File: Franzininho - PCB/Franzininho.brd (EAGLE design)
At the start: 51.6 x 24.1 mm, 16 parts, among them IC1 TINY45-20-DIP, X1 USBPCB

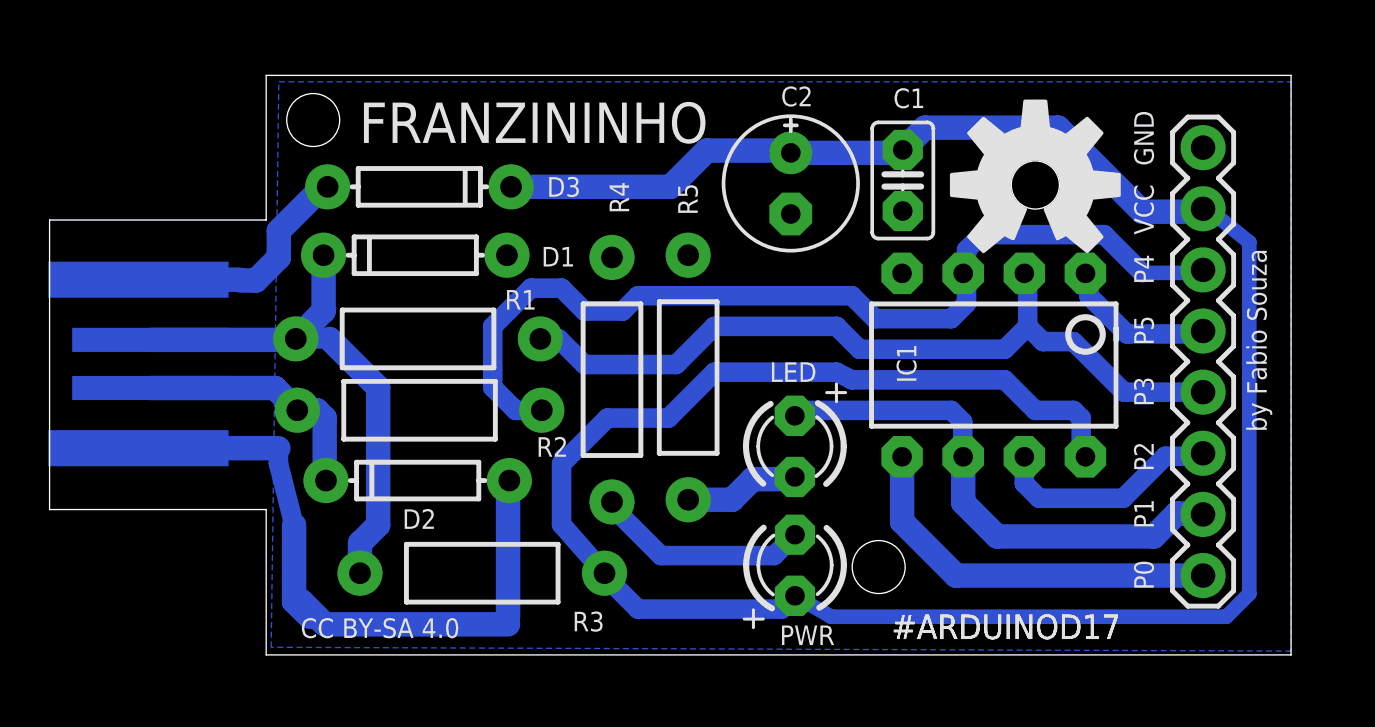
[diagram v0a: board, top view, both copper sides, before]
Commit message: update
aumentado um pouco o tamanho da placa
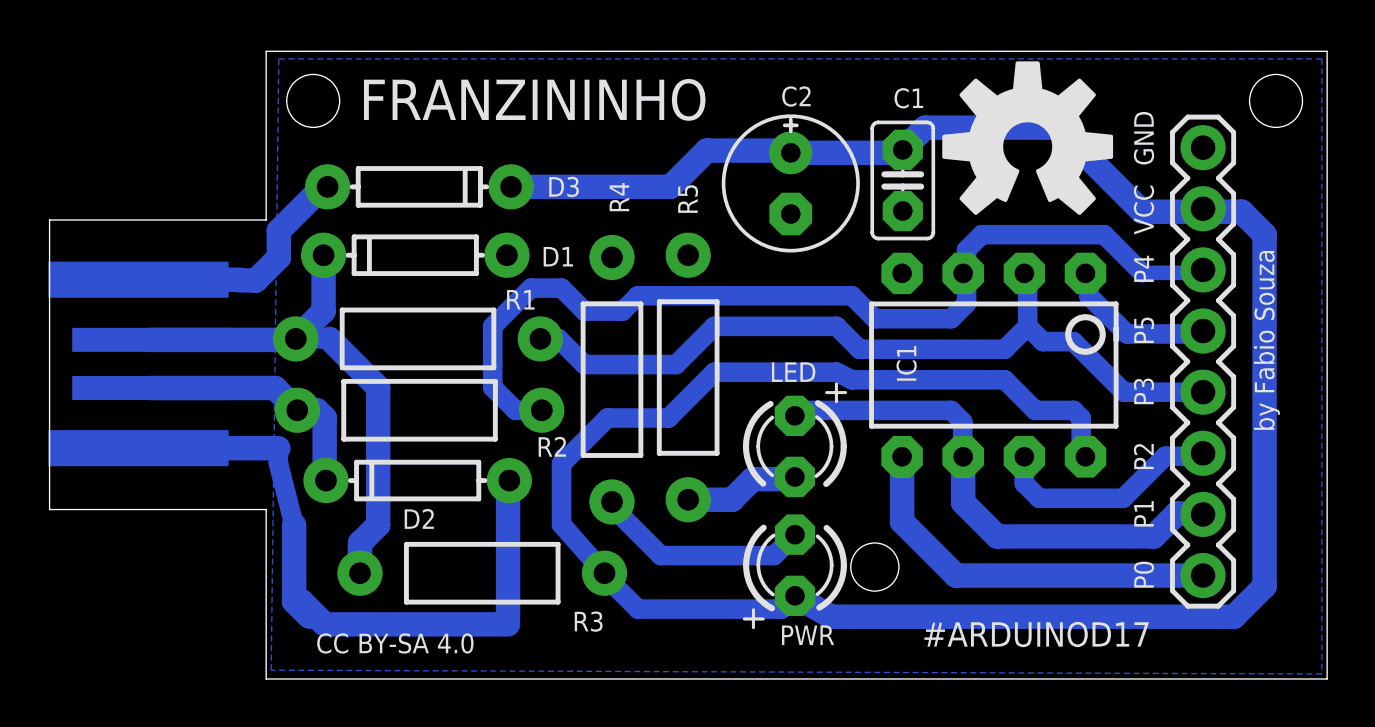
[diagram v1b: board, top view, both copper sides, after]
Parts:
- moved LOGO1 1.62 mm to (40.6, 21.1)
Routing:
- net 5V: track 108.2 -> 110.0 mm
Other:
- board size 51.6 x 24.1 mm -> 53.1 x 26.1 mm
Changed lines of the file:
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@@
 <setting verticaltext="up"/>
 </settings>
-<grid distance="12.5" unitdist="mil" unit="mil" style="lines" multiple="1" display="yes" altdistance="12.5" altunitdist="mil" altunit="mil"/>
+<grid distance="1" unitdist="mm" unit="mm" style="lines" multiple="1" display="yes" altdistance="1" altunitdist="mm" altunit="mm"/>
 <layers>
 <layer number="1" name="Top" color="4" fill="1" visible="no" active="yes"/>
@@
 <plain>
 <wire x1="0" y1="6.04" x2="9" y2="6.04" width="0" layer="20"/>
-<wire x1="9" y1="6.04" x2="9" y2="0" width="0" layer="20"/>
-<wire x1="9" y1="0" x2="51.5825" y2="0" width="0" layer="20"/>
-<wire x1="51.5825" y1="0" x2="51.5825" y2="24.08" width="0" layer="20"/>
-<wire x1="51.5825" y1="24.08" x2="9" y2="24.08" width="0" layer="20"/>
-<wire x1="9" y1="24.08" x2="9" y2="18.07" width="0" layer="20"/>
+<wire x1="9" y1="6.04" x2="9" y2="-1" width="0" layer="20"/>
+<wire x1="9" y1="-1" x2="53.0825" y2="-1" width="0" layer="20"/>
+<wire x1="53.0825" y1="-1" x2="53.0825" y2="25.08" width="0" layer="20"/>
+<wire x1="53.0825" y1="25.08" x2="9" y2="25.08" width="0" layer="20"/>
+<wire x1="9" y1="25.08" x2="9" y2="18.07" width="0" layer="20"/>
 <wire x1="9" y1="18.07" x2="0" y2="18.07" width="0" layer="20"/>
 <wire x1="0" y1="18.07" x2="0" y2="6.04" width="0" layer="20"/>
-<text x="10.42555" y="0.70485" size="0.8128" layer="25" font="vector" ratio="12">CC BY-SA 4.0</text>
-<text x="12.85875" y="21.2725" size="1.6764" layer="25" font="vector" ratio="12" distance="45">FRANZININHO</text>
+<text x="11.06055" y="0.06985" size="0.8128" layer="25" font="vector" ratio="12">CC BY-SA 4.0</text>
+<text x="12.85875" y="22.225" size="1.6764" layer="25" font="vector" ratio="12" distance="45">FRANZININHO</text>
 <text x="45.87875" y="20.32" size="0.8128" layer="25" rot="R90">GND</text>
 <text x="45.87875" y="17.4625" size="0.8128" layer="25" rot="R90">VCC</text>
@@
 <text x="45.87875" y="12.85875" size="0.8128" layer="25" rot="R90">P5</text>
 <text x="45.87875" y="15.39875" size="0.8128" layer="25" rot="R90">P4</text>
-<hole x="10.95375" y="22.225" drill="2.2"/>
-<hole x="34.44875" y="3.65125" drill="2.2"/>
-<text x="44.50195" y="1.6764" size="1.016" layer="25" font="vector" ratio="12" rot="R180">#ARDUINOD17</text>
-<hole x="40.9575" y="19.52625" drill="2"/>
-<text x="44.50195" y="1.6764" size="1.016" layer="25" font="vector" ratio="12" rot="R180">#ARDUINOD17</text>
-<text x="49.7586" y="16.87945" size="0.8128" layer="25" font="vector" ratio="12" rot="R270">by Fabio Souza</text>
+<hole x="10.95375" y="23.01875" drill="2.2"/>
+<hole x="50.95875" y="23.01875" drill="2.2"/>
+<text x="45.77195" y="1.3589" size="1.016" layer="25" font="vector" ratio="12" rot="R180">#ARDUINOD17</text>
+<hole x="34.29" y="3.65125" drill="2"/>
+<text x="50.0761" y="16.87945" size="0.8128" layer="25" font="vector" ratio="12" rot="R270">by Fabio Souza</text>
+<dimension x1="-1" y1="25" x2="-1" y2="-1" x3="-1" y3="12" textsize="1.778" layer="20"/>
+<dimension x1="0" y1="27" x2="53" y2="27" x3="26.5" y3="29" textsize="1.778" layer="20"/>
 </plain>
 <attributes>
@@
 <attribute name="VALUE" x="28.2575" y="16.92275" size="1.27" layer="27" ratio="10" rot="R270"/>
 </element>
-<element name="LOGO1" library="SparkFun-Aesthetics" package="OSHW-LOGO-L" value="OSHW-LOGOL" x="40.9575" y="19.52625"/>
+<element name="LOGO1" library="SparkFun-Aesthetics" package="OSHW-LOGO-L" value="OSHW-LOGOL" x="40.64" y="21.11375"/>
 </elements>
 <signals>
@@
 <contactref element="C2" pad="-"/>
 <polygon width="0.3048" layer="16" isolate="0.4572">
-<vertex x="9.525" y="23.8125"/>
-<vertex x="51.59375" y="23.8125"/>
-<vertex x="51.59375" y="0.15875"/>
-<vertex x="9.2075" y="0.3175"/>
+<vertex x="9.525" y="24.765"/>
+<vertex x="52.86375" y="24.765"/>
+<vertex x="52.86375" y="-0.79375"/>
+<vertex x="9.2075" y="-0.635"/>
 </polygon>
 <contactref element="JP3" pad="8"/>
@@
 <wire x1="45.4025" y1="18.415" x2="48.28125" y2="18.415" width="1.016" layer="16"/>
 <wire x1="48.28125" y1="18.415" x2="47.9275" y2="18.5375" width="0.4064" layer="16"/>
-<wire x1="48.28125" y1="18.415" x2="49.8475" y2="17.145" width="0.6096" layer="16"/>
-<wire x1="49.8475" y1="17.145" x2="49.8475" y2="2.54" width="0.6096" layer="16"/>
-<wire x1="49.8475" y1="2.54" x2="48.895" y2="1.5875" width="0.6096" layer="16"/>
-<wire x1="48.895" y1="1.5875" x2="32.476" y2="1.5875" width="0.6096" layer="16"/>
-<wire x1="32.476" y1="1.5875" x2="30.9725" y2="2.456" width="0.6096" layer="16"/>
+<wire x1="49.2125" y1="1.5875" x2="32.476" y2="1.5875" width="1.016" layer="16"/>
+<wire x1="32.476" y1="1.5875" x2="30.9725" y2="2.456" width="1.016" layer="16"/>
 <wire x1="19.1741" y1="19.4481" x2="25.7981" y2="19.4481" width="1.016" layer="16"/>
 <wire x1="25.7981" y1="19.4481" x2="27.305" y2="20.955" width="1.016" layer="16"/>
@@
 <wire x1="30.4215" y1="1.905" x2="30.9725" y2="2.456" width="0.8128" layer="16"/>
 <wire x1="27.6225" y1="11.7475" x2="32.7025" y2="11.7475" width="0.8128" layer="16"/>
+<wire x1="49.2125" y1="1.5875" x2="50.4825" y2="2.8575" width="1.016" layer="16"/>
+<wire x1="50.4825" y1="2.8575" x2="50.4825" y2="17.4625" width="1.016" layer="16"/>
+<wire x1="50.4825" y1="17.4625" x2="49.53" y2="18.415" width="1.016" layer="16"/>
+<wire x1="49.53" y1="18.415" x2="48.05" y2="18.415" width="1.016" layer="16"/>
+<wire x1="48.05" y1="18.415" x2="47.9275" y2="18.5375" width="1.016" layer="16"/>
 </signal>
 <signal name="N$1">

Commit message: layout
Melhorias no Layout
BOM
Nova imagem da placa com melhor resolução e cotas
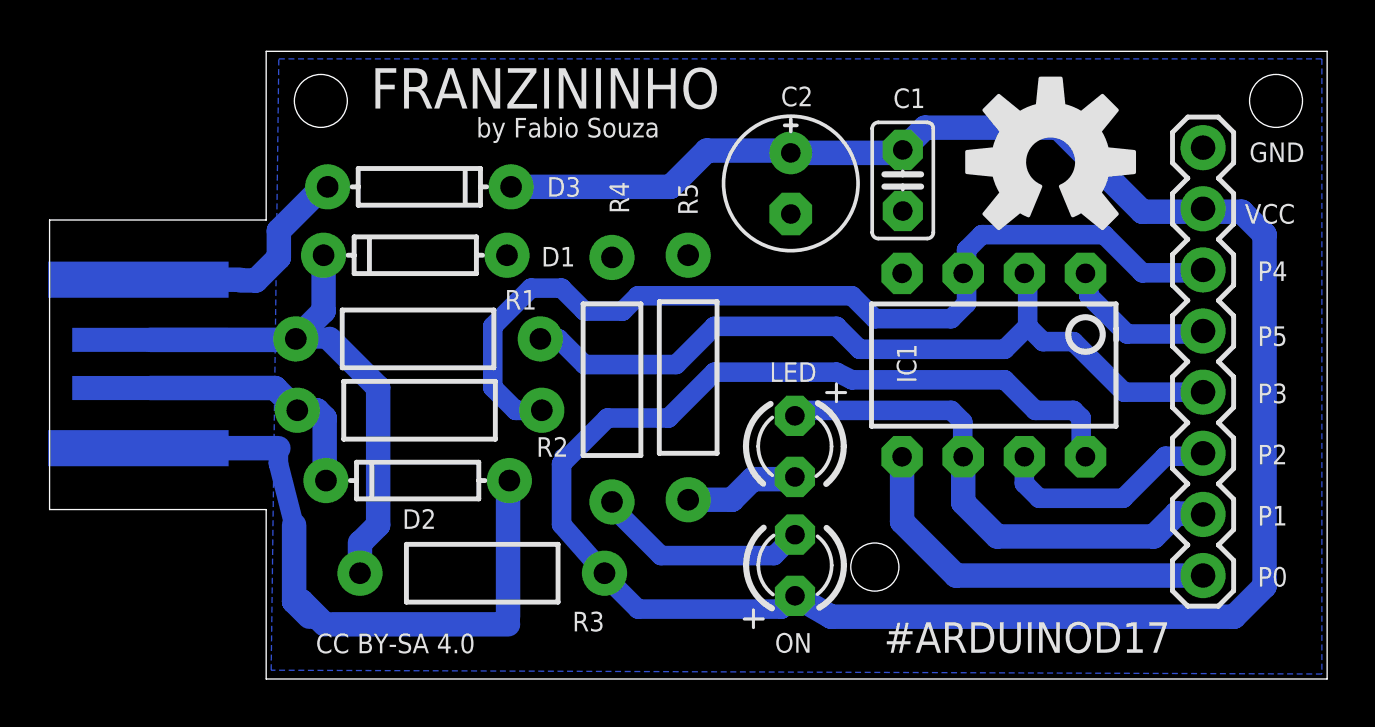
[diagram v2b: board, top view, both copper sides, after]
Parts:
- moved LOGO1 1.14 mm to (41.6, 20.5)
- renumbered PWR to ON
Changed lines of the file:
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@@
 <setting verticaltext="up"/>
 </settings>
-<grid distance="1" unitdist="mm" unit="mm" style="lines" multiple="1" display="yes" altdistance="1" altunitdist="mm" altunit="mm"/>
+<grid distance="12.5" unitdist="mil" unit="mil" style="lines" multiple="1" display="yes" altdistance="12.5" altunitdist="mil" altunit="mil"/>
 <layers>
 <layer number="1" name="Top" color="4" fill="1" visible="no" active="yes"/>
@@
 <layer number="49" name="Reference" color="7" fill="1" visible="yes" active="yes"/>
 <layer number="50" name="dxf" color="7" fill="1" visible="no" active="no"/>
-<layer number="51" name="tDocu" color="7" fill="1" visible="yes" active="yes"/>
+<layer number="51" name="tDocu" color="7" fill="1" visible="no" active="yes"/>
 <layer number="52" name="bDocu" color="7" fill="1" visible="no" active="yes"/>
 <layer number="53" name="tGND_GNDA" color="7" fill="9" visible="no" active="no"/>
@@
 <wire x1="9" y1="18.07" x2="0" y2="18.07" width="0" layer="20"/>
 <wire x1="0" y1="18.07" x2="0" y2="6.04" width="0" layer="20"/>
-<text x="11.06055" y="0.06985" size="0.8128" layer="25" font="vector" ratio="12">CC BY-SA 4.0</text>
-<text x="12.85875" y="22.225" size="1.6764" layer="25" font="vector" ratio="12" distance="45">FRANZININHO</text>
-<text x="45.87875" y="20.32" size="0.8128" layer="25" rot="R90">GND</text>
-<text x="45.87875" y="17.4625" size="0.8128" layer="25" rot="R90">VCC</text>
-<text x="45.87875" y="2.69875" size="0.8128" layer="25" rot="R90">P0</text>
-<text x="45.87875" y="5.23875" size="0.8128" layer="25" rot="R90">P1</text>
-<text x="45.87875" y="7.62" size="0.8128" layer="25" rot="R90">P2</text>
-<text x="45.87875" y="10.31875" size="0.8128" layer="25" rot="R90">P3</text>
-<text x="45.87875" y="12.85875" size="0.8128" layer="25" rot="R90">P5</text>
-<text x="45.87875" y="15.39875" size="0.8128" layer="25" rot="R90">P4</text>
-<hole x="10.95375" y="23.01875" drill="2.2"/>
+<text x="11.06055" y="0.06985" size="0.8128" layer="25" font="vector" ratio="15">CC BY-SA 4.0</text>
+<text x="13.335" y="22.70125" size="1.6764" layer="25" font="vector" ratio="12" distance="45">FRANZININHO</text>
+<text x="49.8475" y="20.47875" size="0.8128" layer="25">GND</text>
+<text x="51.7525" y="18.7325" size="0.8128" layer="25" rot="R180">VCC</text>
+<text x="51.435" y="3.65125" size="0.8128" layer="25" rot="R180">P0</text>
+<text x="51.435" y="6.19125" size="0.8128" layer="25" rot="R180">P1</text>
+<text x="51.435" y="8.73125" size="0.8128" layer="25" rot="R180">P2</text>
+<text x="51.435" y="11.27125" size="0.8128" layer="25" rot="R180">P3</text>
+<text x="51.435" y="13.6525" size="0.8128" layer="25" rot="R180">P5</text>
+<text x="51.435" y="16.35125" size="0.8128" layer="25" rot="R180">P4</text>
+<hole x="11.27125" y="23.01875" drill="2.2"/>
 <hole x="50.95875" y="23.01875" drill="2.2"/>
-<text x="45.77195" y="1.3589" size="1.016" layer="25" font="vector" ratio="12" rot="R180">#ARDUINOD17</text>
+<text x="46.5657" y="1.3589" size="1.27" layer="25" font="vector" ratio="12" rot="R180">#ARDUINOD17</text>
 <hole x="34.29" y="3.65125" drill="2"/>
-<text x="50.0761" y="16.87945" size="0.8128" layer="25" font="vector" ratio="12" rot="R270">by Fabio Souza</text>
-<dimension x1="-1" y1="25" x2="-1" y2="-1" x3="-1" y3="12" textsize="1.778" layer="20"/>
-<dimension x1="0" y1="27" x2="53" y2="27" x3="26.5" y3="29" textsize="1.778" layer="20"/>
+<text x="17.72805" y="21.5011" size="0.8128" layer="25" font="vector" ratio="12">by Fabio Souza</text>
+<dimension x1="-1" y1="25" x2="-1" y2="-1" x3="-1" y3="12" textsize="1.778" layer="51"/>
+<dimension x1="0" y1="27" x2="53" y2="27" x3="26.5" y3="29" textsize="1.778" layer="51"/>
+<dimension x1="9" y1="25.08" x2="53" y2="25" x3="31.00538125" y3="27.999990625" textsize="1.778" layer="150"/>
+<dimension x1="0" y1="18.07" x2="53" y2="18" x3="26.5277375" y3="39.037603125" textsize="1.778" layer="150"/>
+<dimension x1="53.0825" y1="25.08" x2="53" y2="-1" x3="66.03163125" y3="11.99890625" textsize="1.778" layer="150"/>
+<dimension x1="0" y1="18.07" x2="0" y2="6" x3="-4" y3="12.035" textsize="1.778" layer="150"/>
+<dimension x1="0" y1="6.04" x2="9" y2="6.04" x3="4.5" y3="-8" textsize="1.778" layer="150"/>
 </plain>
 <attributes>
@@
 <attribute name="PROD_ID" value="DIO-08378" x="15.3641" y="19.4481" size="1.778" layer="27" display="off"/>
 </element>
-<element name="PWR" library="adafruit" package="LED3MM" value="" x="30.9725" y="3.726" smashed="yes" rot="R90">
-<attribute name="NAME" x="32.62775" y="1.22275" size="0.8128" layer="25" font="vector" ratio="10" rot="R180"/>
+<element name="ON" library="adafruit" package="LED3MM" value="" x="30.9725" y="3.726" smashed="yes" rot="R90">
+<attribute name="NAME" x="31.67525" y="0.90525" size="0.8128" layer="25" font="vector" ratio="10" rot="R180"/>
 <attribute name="VALUE" x="32.6235" y="5.631" size="1.27" layer="27" ratio="10" rot="R90"/>
 </element>
@@
 <attribute name="VALUE" x="28.2575" y="16.92275" size="1.27" layer="27" ratio="10" rot="R270"/>
 </element>
-<element name="LOGO1" library="SparkFun-Aesthetics" package="OSHW-LOGO-L" value="OSHW-LOGOL" x="40.64" y="21.11375"/>
+<element name="LOGO1" library="SparkFun-Aesthetics" package="OSHW-LOGO-L" value="OSHW-LOGOL" x="41.5925" y="20.47875"/>
 </elements>
 <signals>
@@
 <contactref element="C1" pad="2"/>
 <contactref element="C2" pad="-"/>
-<polygon width="0.3048" layer="16" isolate="0.4572">
+<polygon width="0.0254" layer="16" isolate="0.4572">
 <vertex x="9.525" y="24.765"/>
 <vertex x="52.86375" y="24.765"/>
@@
 <contactref element="IC1" pad="8"/>
 <contactref element="R3" pad="P$1"/>
-<contactref element="PWR" pad="A"/>
+<contactref element="ON" pad="A"/>
 <contactref element="C1" pad="1"/>
 <contactref element="C2" pad="+"/>
@@
 <wire x1="38.735" y1="17.4625" x2="43.815" y2="17.4625" width="0.8128" layer="16"/>
 <wire x1="43.815" y1="17.4625" x2="45.4025" y2="15.875" width="0.8128" layer="16"/>
-<wire x1="45.4025" y1="15.875" x2="47.805" y2="15.875" width="0.6096" layer="16"/>
+<wire x1="45.4025" y1="15.875" x2="47.805" y2="15.875" width="0.8128" layer="16"/>
 <wire x1="47.805" y1="15.875" x2="47.9275" y2="15.9975" width="0.4064" layer="16"/>
 <wire x1="20.0025" y1="15.24" x2="18.415" y2="13.6525" width="0.8128" layer="16"/>
@@
 </signal>
 <signal name="N$17">
-<contactref element="PWR" pad="K"/>
+<contactref element="ON" pad="K"/>
 <contactref element="R4" pad="P$2"/>
 <wire x1="23.3685" y1="6.3555" x2="23.3685" y2="6.159" width="0.4064" layer="16"/>

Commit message: atualização de arquivos
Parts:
- IC1: value TINY45-20-DIP -> ATTINY85 - 20PU
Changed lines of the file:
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@@
 <layer number="21" name="tPlace" color="7" fill="1" visible="yes" active="yes"/>
 <layer number="22" name="bPlace" color="7" fill="1" visible="no" active="yes"/>
-<layer number="23" name="tOrigins" color="15" fill="1" visible="yes" active="yes"/>
-<layer number="24" name="bOrigins" color="15" fill="1" visible="yes" active="yes"/>
+<layer number="23" name="tOrigins" color="15" fill="1" visible="no" active="yes"/>
+<layer number="24" name="bOrigins" color="15" fill="1" visible="no" active="yes"/>
 <layer number="25" name="tNames" color="7" fill="1" visible="yes" active="yes"/>
 <layer number="26" name="bNames" color="7" fill="1" visible="no" active="yes"/>
@@
 <layer number="132" name="bAdjust" color="7" fill="1" visible="yes" active="yes"/>
 <layer number="144" name="Drill_legend" color="7" fill="1" visible="no" active="yes"/>
-<layer number="150" name="Notes" color="7" fill="1" visible="yes" active="yes"/>
+<layer number="150" name="Notes" color="7" fill="1" visible="no" active="yes"/>
 <layer number="151" name="HeatSink" color="7" fill="1" visible="no" active="yes"/>
 <layer number="152" name="_bDocu" color="7" fill="1" visible="yes" active="yes"/>
@@
 <attribute name="VALUE" x="2.62" y="17.17" size="0.4064" layer="28" rot="MR180"/>
 </element>
-<element name="IC1" library="SparkFun-DigitalIC" package="DIP08" value="TINY45-20-DIP" x="39.2316" y="12.0435" smashed="yes" rot="R180">
+<element name="IC1" library="SparkFun-DigitalIC" package="DIP08" value="ATTINY85 - 20PU" x="39.2316" y="12.0435" smashed="yes" rot="R180">
 <attribute name="PROD_ID" value="IC-09439" x="39.2316" y="12.0435" size="1.778" layer="27" rot="R180" display="off"/>
 <attribute name="VALUE" value="TINY45-20-DIP" x="39.2316" y="12.0435" size="1.778" layer="27" rot="R180" display="off"/>
@@
 <contactref element="C1" pad="2"/>
 <contactref element="C2" pad="-"/>
-<polygon width="0.0254" layer="16" isolate="0.4572">
+<polygon width="0.0254" layer="16" isolate="0.4572" thermals="no">
 <vertex x="9.525" y="24.765"/>
 <vertex x="52.86375" y="24.765"/>
